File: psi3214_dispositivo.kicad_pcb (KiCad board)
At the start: 2 copper layers, 51.5 x 67 mm, 30 parts, among them J10 Conn_01x01, J2 AudioJack3, J4 Conn_01x03, J5 AudioJack3, J6 Conn_01x01, J7 Conn_01x01, J8 Conn_01x01, J9 Conn_01x01, U1 TL072_sim, U2 MAX1044

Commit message: Done
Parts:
- moved J6 96.1 mm to (141.0, 125.5)
- moved J9 89.5 mm to (139.5, 103.0)
- moved J10 85.0 mm to (148.5, 72.5)
- moved J8 76.9 mm to (153.0, 106.5)
- moved J7 66.7 mm to (164.5, 107.5)
- moved J4 0.50 mm to (164.0, 72.5)
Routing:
- net entrada: track 15.4 -> 21.4 mm
- net saida: track 81.2 -> 86.2 mm
- net saida_cap: track 28.3 -> 32.2 mm
- net saida_amp1: track 43.5 -> 45.0 mm
- net saida_filtro: vias 2 -> 0
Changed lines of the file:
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@@
 	(footprint "TestPoint:TestPoint_Pad_1.5x1.5mm"
 		(layer "F.Cu")
-		(at 228.775 100.475)
+		(at 148.5 72.5)
 		(descr "SMD rectangular pad as test Point, square 1.5mm side length")
 		(tags "test point SMD pad rectangle square")
@@
 	(footprint "TestPoint:TestPoint_Pad_1.5x1.5mm"
 		(layer "F.Cu")
-		(at 228.775 96.925)
+		(at 139.5 103)
 		(descr "SMD rectangular pad as test Point, square 1.5mm side length")
 		(tags "test point SMD pad rectangle square")
@@
 	(footprint "TerminalBlock:TerminalBlock_MaiXu_MX126-5.0-03P_1x03_P5.00mm"
 		(layer "F.Cu")
-		(at 164 72 180)
+		(at 164 72.5 180)
 		(descr "terminal block MaiXu MX126-5.0-03P, 3 pins, pitch 5mm, size 15.5x7.8mm, drill diameter 1.3mm, pad diameter 2.8mm, https://www.lcsc.com/datasheet/lcsc_datasheet_2309150913_MAX-MX126-5-0-03P-GN01-Cu-S-A_C5188435.pdf")
 		(tags "THT terminal block MaiXu MX126-5.0-03P pitch 5mm size 15.5x7.8mm drill 1.3mm pad 2.8mm")
@@
 	(footprint "TestPoint:TestPoint_Pad_1.5x1.5mm"
 		(layer "F.Cu")
-		(at 228.775 89.825)
+		(at 164.5 107.5)
 		(descr "SMD rectangular pad as test Point, square 1.5mm side length")
 		(tags "test point SMD pad rectangle square")
@@
 	(footprint "TestPoint:TestPoint_Pad_1.5x1.5mm"
 		(layer "F.Cu")
-		(at 228.775 86.275)
+		(at 141 125.5)
 		(descr "SMD rectangular pad as test Point, square 1.5mm side length")
 		(tags "test point SMD pad rectangle square")
@@
 	(footprint "TestPoint:TestPoint_Pad_1.5x1.5mm"
 		(layer "F.Cu")
-		(at 228.775 93.375)
+		(at 153 106.5)
 		(descr "SMD rectangular pad as test Point, square 1.5mm side length")
 		(tags "test point SMD pad rectangle square")
@@
 		(tags "9V Battery Holder")
 		(property "Reference" "BT1"
-			(at -24.13 24.13 90)
+			(at 1.575 22.975 90)
 			(layer "B.SilkS")
 			(effects
@@
 		)
 		(fill no)
-		(locked yes)
 		(layer "Edge.Cuts")
 	)
@@
 	)
 	(segment
+		(start 144.94 76.06)
+		(end 144.94 77)
+		(width 0.5)
+		(layer "F.Cu")
+		(net "entrada")
+	)
+	(segment
 		(start 133.75625 77)
 		(end 131.75625 79)
@@
 	)
 	(segment
+		(start 148.5 72.5)
+		(end 144.94 76.06)
+		(width 0.5)
+		(layer "F.Cu")
+		(net "entrada")
+	)
+	(segment
 		(start 158.742501 88)
 		(end 157.73 89.012501)
@@
 	)
 	(segment
+		(start 139.5 103)
+		(end 140.46 102.04)
+		(width 0.5)
+		(layer "F.Cu")
+		(net "saida_cap")
+	)
+	(segment
+		(start 140.46 102.04)
+		(end 143.025 102.04)
+		(width 0.5)
+		(layer "F.Cu")
+		(net "saida_cap")
+	)
+	(segment
 		(start 131.74375 81.9375)
 		(end 131.75625 81.95)
@@
 	)
 	(segment
+		(start 153 106.5)
+		(end 153 107.95)
+		(width 0.5)
+		(layer "F.Cu")
+		(net "saida_amp1")
+	)
+	(segment
 		(start 148.95 107.95)
-		(end 156.74375 107.95)
+		(end 153 107.95)
 		(width 0.5)
 		(layer "F.Cu")
@@
 	)
 	(segment
+		(start 153 107.95)
+		(end 156.74375 107.95)
+		(width 0.5)
+		(layer "F.Cu")
+		(net "saida_amp1")
+	)
+	(segment
 		(start 143.025 99.5)
 		(end 143.999999 99.5)
@@
 		(net "saida_filtro")
 	)
-	(via
-		(at 156.74375 104.95)
-		(size 1.3)
-		(drill 1)
-		(layers "F.Cu" "B.Cu")
-		(net "saida_filtro")
-	)
-	(via
-		(at 148.5 103.405)
-		(size 1.3)
-		(drill 1)
-		(layers "F.Cu" "B.Cu")
-		(net "saida_filtro")
-	)
 	(segment
 		(start 164.603122 95.5)
@@
 	)
 	(segment
+		(start 146 125.5375)
+		(end 145.9625 125.5375)
+		(width 0.5)
+		(layer "F.Cu")
+		(net "saida")
+	)
+	(segment
 		(start 147.975 100.77)
 		(end 159.333122 100.77)
@@
 	)
 	(segment
+		(start 145.9625 125.5375)
+		(end 145.925 125.5)
+		(width 0.5)
+		(layer "F.Cu")
+		(net "saida")
+	)
+	(segment
+		(start 145.925 125.5)
+		(end 141 125.5)
+		(width 0.5)
+		(layer "F.Cu")
+		(net "saida")
+	)
+	(segment
 		(start 159.333122 100.77)
 		(end 164.603122 95.5)
@@
 	(group ""
 		(members "14745f03-05dc-4cd0-89e9-776f34363ecf" "154efa24-01ee-48c5-b3e4-0f4ca531b3f0"
-			"1aee159e-6702-4bb1-bde7-9e6e1884ac13" "1c8acdb6-b4c1-4064-b114-e656a947514a"
-			"22fa1173-741b-4381-8e74-b86ff30d0945" "2b0b8234-6164-466c-b652-52a971f39395"
-			"2b41dde3-c84d-4543-9a96-1787f0b285c1" "2f28cfff-f9f9-43be-8797-b2e1f59ad7bc"
-			"343e6841-0d4a-4e79-a3b2-7967d0d20163" "3f3f7c97-fcaa-4079-a980-4427889126a4"
-			"480a5ed7-1af6-4619-90ff-798dfbfb77f7" "61958a5a-42b2-491c-b865-d1ced87ccc9f"
-			"8082b6f6-f100-4bf7-8dc4-07182a355fea" "8126957b-73c6-444a-be5d-9f791a7acc27"
-			"8d18a215-3aeb-4023-95dd-b77dcca60d59" "905a92f3-83ed-4ffa-8d1c-a3bbd837412f"
-			"951aaebe-c3ef-44f2-a0cf-6d5fad2ed7f6" "a73f8800-e95f-4d06-be44-a1240b0fc3cc"
-			"b6a62179-4b03-40ff-8bab-689c47c05c9e" "b8a28bca-1def-49ac-ad3c-ae58ddc642b4"
-			"bafb4bf0-64e9-47ca-8ece-63d6f56b0ff9" "c1de1c94-089c-41dd-a395-84eb7719ef45"
-			"ec63bb98-5a18-424b-b821-08472d7126e0" "f0c0485d-5035-4d05-96e7-1607e698c647"
-			"facedce3-9cf7-44b6-9869-26feb8a5123d"
+			"1aee159e-6702-4bb1-bde7-9e6e1884ac13" "22fa1173-741b-4381-8e74-b86ff30d0945"
+			"2b0b8234-6164-466c-b652-52a971f39395" "2b41dde3-c84d-4543-9a96-1787f0b285c1"
+			"2f28cfff-f9f9-43be-8797-b2e1f59ad7bc" "343e6841-0d4a-4e79-a3b2-7967d0d20163"
+			"3f3f7c97-fcaa-4079-a980-4427889126a4" "480a5ed7-1af6-4619-90ff-798dfbfb77f7"
+			"61958a5a-42b2-491c-b865-d1ced87ccc9f" "8082b6f6-f100-4bf7-8dc4-07182a355fea"
+			"8126957b-73c6-444a-be5d-9f791a7acc27" "8d18a215-3aeb-4023-95dd-b77dcca60d59"
+			"905a92f3-83ed-4ffa-8d1c-a3bbd837412f" "951aaebe-c3ef-44f2-a0cf-6d5fad2ed7f6"
+			"a73f8800-e95f-4d06-be44-a1240b0fc3cc" "b6a62179-4b03-40ff-8bab-689c47c05c9e"
+			"b8a28bca-1def-49ac-ad3c-ae58ddc642b4" "bafb4bf0-64e9-47ca-8ece-63d6f56b0ff9"
+			"c1de1c94-089c-41dd-a395-84eb7719ef45" "ec63bb98-5a18-424b-b821-08472d7126e0"
+			"f0c0485d-5035-4d05-96e7-1607e698c647" "facedce3-9cf7-44b6-9869-26feb8a5123d"
 		)
 	)
@@
 		(members "27194d6a-d355-4282-ae18-7fcf0f1794ac" "2b4fa705-d409-477f-9120-7bdad3f1d6c2"
 			"46ea5ecc-d7cb-4b33-b120-8154e6843f22" "50b699a6-7df6-46d9-b706-60c5ef60eb3c"
-			"7c33bc94-0567-4c22-8bc7-edf92cc4cd55" "9003614e-ef1e-4317-b11f-7afc45a6426e"
-			"a28c9a9a-03d4-4565-8e0c-1bf621f61360" "c4dd5917-c9f5-4bf1-9a05-7b9d8135a8d8"
-			"dffe39d6-6ec0-4260-8ec6-5e965079c3a3"
+			"7c33bc94-0567-4c22-8bc7-edf92cc4cd55" "a28c9a9a-03d4-4565-8e0c-1bf621f61360"
+			"c4dd5917-c9f5-4bf1-9a05-7b9d8135a8d8" "dffe39d6-6ec0-4260-8ec6-5e965079c3a3"
 		)
 	)

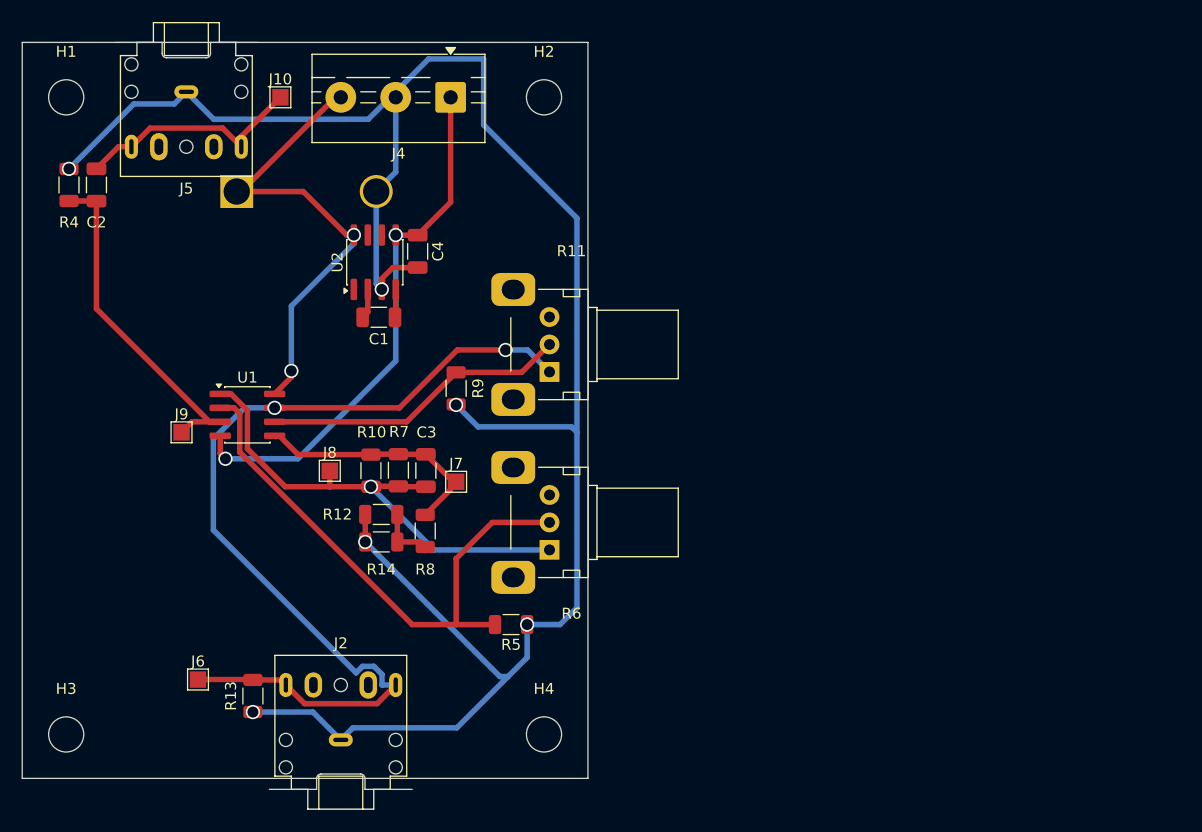
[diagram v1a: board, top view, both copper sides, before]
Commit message: Edge.Cuts audio_jack fix and project params correct
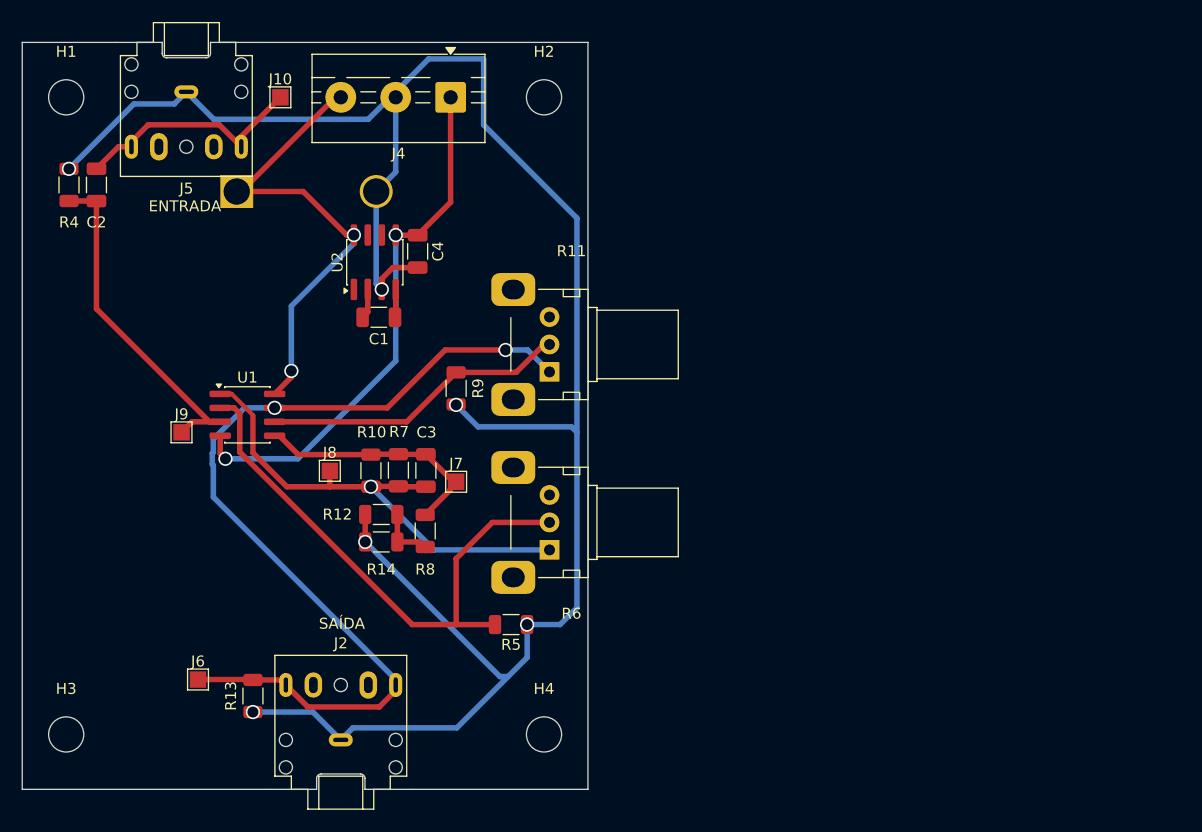
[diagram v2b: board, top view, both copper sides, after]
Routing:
- net saida: track 86.2 -> 84.3 mm
- net entrada: track 21.4 -> 21.9 mm
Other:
- board size 51.5 x 67 mm -> 51.5 x 68 mm
- board text added: "ENTRADA"
- board text added: "SAÍDA"
